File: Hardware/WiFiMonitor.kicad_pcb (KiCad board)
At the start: 2 copper layers, 47.2 x 47.1 mm, 41 parts, among them J1 ADAP_ESP, J2 FTDI, J3 BATT, U1 4N25, U2 4N25, U3 4N25, U4 4N25, U5 U5, U6 AP1117-33, U7 DS3231MZ+

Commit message: pads3
move
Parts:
- moved IN2 0.35 mm to (145.6, 97.8), turned to 136 degrees
- moved COM2 0.09 mm to (154.7, 84.7), turned to 134 degrees
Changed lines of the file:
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@@
     (area 125.549999 67.068854 174.355 116.145)
     (thickness 1.6)
-    (drawings 30)
-    (tracks 632)
+    (drawings 28)
+    (tracks 634)
     (zones 0)
     (modules 41)
@@
   )
   (module PADS:PAD_4X2mmTH (layer F.Cu)
-    (at 145.92 97.67 145)
-    (fp_text reference IN2 (at 0 2.5 145) (layer F.SilkS)
+    (at 145.59 97.8 136)
+    (fp_text reference IN2 (at 0 2.5 136) (layer F.SilkS)
       (effects (font (size 1 1) (thickness 0.15)))
     )
-    (fp_text value 1_IN (at 0 -2.5 145) (layer F.Fab)
+    (fp_text value 1_IN (at 0 -2.5 136) (layer F.Fab)
       (effects (font (size 1 1) (thickness 0.15)))
     )
-    (pad 1 thru_hole rect (at 0 0 145) (size 5 2) (drill oval 3.25 0.78) (layers *.Cu *.Mask)
+    (pad 1 thru_hole rect (at 0 0 136) (size 5 2) (drill oval 3.25 0.78) (layers *.Cu *.Mask)
       (net 11 "Net-(IN2-Pad1)"))
   )
@@
   )
   (module PADS:PAD_4X2mmTH (layer F.Cu)
-    (at 154.59 84.66 133)
-    (fp_text reference COM2 (at 0.082226 -2.078975 133) (layer F.SilkS)
+    (at 154.66 84.72 134)
+    (fp_text reference COM2 (at 0.082226 -2.078975 134) (layer F.SilkS)
       (effects (font (size 1 1) (thickness 0.15)))
     )
-    (fp_text value TORRETA (at 0 -2.5 133) (layer F.Fab)
+    (fp_text value TORRETA (at 0 -2.5 134) (layer F.Fab)
       (effects (font (size 1 1) (thickness 0.15)))
     )
-    (pad 1 thru_hole rect (at 0 0 133) (size 5 2) (drill oval 3.25 0.78) (layers *.Cu *.Mask)
+    (pad 1 thru_hole rect (at 0 0 134) (size 5 2) (drill oval 3.25 0.78) (layers *.Cu *.Mask)
       (net 6 GNDA))
   )
@@
     )
   )
-  (dimension 10.120835 (width 0.3) (layer Margin)
-    (gr_text "10.121 mm" (at 150.245462 94.674818 0.7359724973) (layer Margin)
-      (effects (font (size 1.5 1.5) (thickness 0.3)))
-    )
-    (feature1 (pts (xy 145.21 96.65) (xy 145.168122 93.38993)))
-    (feature2 (pts (xy 155.33 96.52) (xy 155.288122 93.25993)))
-    (crossbar (pts (xy 155.322803 95.959707) (xy 145.202803 96.089707)))
-    (arrow1a (pts (xy 145.202803 96.089707) (xy 146.321681 95.488865)))
-    (arrow1b (pts (xy 145.202803 96.089707) (xy 146.336746 96.66161)))
-    (arrow2a (pts (xy 155.322803 95.959707) (xy 154.18886 95.387804)))
-    (arrow2b (pts (xy 155.322803 95.959707) (xy 154.203925 96.560549)))
-  )
-  (dimension 5.11 (width 0.3) (layer Margin)
-    (gr_text "5 mm" (at 150.435 96.56) (layer Margin)
-      (effects (font (size 1.5 1.5) (thickness 0.3)))
-    )
-    (feature1 (pts (xy 147.88 98.58) (xy 147.88 95.21)))
-    (feature2 (pts (xy 152.99 98.58) (xy 152.99 95.21)))
-    (crossbar (pts (xy 152.99 97.91) (xy 147.88 97.91)))
-    (arrow1a (pts (xy 147.88 97.91) (xy 149.006504 97.323579)))
-    (arrow1b (pts (xy 147.88 97.91) (xy 149.006504 98.496421)))
-    (arrow2a (pts (xy 152.99 97.91) (xy 151.863496 97.323579)))
-    (arrow2b (pts (xy 152.99 97.91) (xy 151.863496 98.496421)))
-  )
   (gr_circle (center 149.85 91.06) (end 151.05 94.37) (layer Edge.Cuts) (width 0.2))
   (gr_circle (center 149.86 91.03) (end 153.19 93.27) (layer Margin) (width 0.2))
@@
   (segment (start 153.62 103.55) (end 155.175 103.55) (width 0.3) (layer B.Cu) (net 10))
   (segment (start 153.62 103.55) (end 154.95 103.55) (width 0.3) (layer B.Cu) (net 10))
+  (segment (start 144.44 99.15) (end 144.44 98.95) (width 0.3) (layer F.Cu) (net 11))
+  (segment (start 144.44 98.95) (end 145.59 97.8) (width 0.3) (layer F.Cu) (net 11))
   (segment (start 145.972894 101.89) (end 144.44 100.357106) (width 0.3) (layer F.Cu) (net 11))
   (segment (start 144.44 100.357106) (end 144.44 99.15) (width 0.3) (layer F.Cu) (net 11))
-  (segment (start 144.44 99.15) (end 145.92 97.67) (width 0.3) (layer F.Cu) (net 11))
   (segment (start 146.68 101.89) (end 145.972894 101.89) (width 0.3) (layer F.Cu) (net 11))
   (via (at 146.68 101.89) (size 1) (drill 0.4) (layers F.Cu B.Cu) (net 11))
@@
   (segment (start 135.53 103.045) (end 136.8206 103.045) (width 0.3) (layer F.Cu) (net 22))
   (segment (start 136.8206 103.045) (end 136.8356 103.06) (width 0.3) (layer F.Cu) (net 22))
-  (segment (start 160.23 93.59) (end 160.23 84.56) (width 0.3) (layer F.Cu) (net 23))
-  (segment (start 160.23 84.56) (end 159.86 84.19) (width 0.3) (layer F.Cu) (net 23))
-  (segment (start 159.86 84.19) (end 159.86 75.9) (width 0.3) (layer F.Cu) (net 23))
-  (segment (start 163.69 98.88) (end 160.23 95.42) (width 0.3) (layer B.Cu) (net 23))
-  (segment (start 160.23 95.42) (end 160.23 93.59) (width 0.3) (layer B.Cu) (net 23))
-  (via (at 160.23 93.59) (size 1) (drill 0.4) (layers F.Cu B.Cu) (net 23))
-  (segment (start 163.69 98.98) (end 163.69 98.88) (width 0.3) (layer B.Cu) (net 23))
   (segment (start 143.51 106.21) (end 144.61 106.21) (width 0.3) (layer B.Cu) (net 23))
-  (segment (start 144.61 106.21) (end 145.11 105.71) (width 0.3) (layer B.Cu) (net 23))
   (segment (start 145.11 105.71) (end 145.11 101.765) (width 0.3) (layer B.Cu) (net 23))
-  (segment (start 163.25 100.58) (end 163.69 100.14) (width 0.3) (layer B.Cu) (net 23))
-  (segment (start 145.11 101.765) (end 146.16 100.715) (width 0.3) (layer B.Cu) (net 23))
-  (segment (start 146.16 100.715) (end 153.885 100.715) (width 0.3) (layer B.Cu) (net 23))
-  (segment (start 154.86 99.74) (end 158 99.74) (width 0.3) (layer B.Cu) (net 23))
-  (segment (start 153.885 100.715) (end 154.86 99.74) (width 0.3) (layer B.Cu) (net 23))
+  (segment (start 144.61 106.21) (end 145.11 105.71) (width 0.3) (layer B.Cu) (net 23))
+  (segment (start 150.52789 100.86499) (end 153.73501 100.86499) (width 0.3) (layer B.Cu) (net 23))
+  (segment (start 160.23 95.42) (end 160.23 93.59) (width 0.3) (layer B.Cu) (net 23))
+  (segment (start 145.11 101.765) (end 145.945 100.93) (width 0.3) (layer B.Cu) (net 23))
+  (segment (start 145.945 100.93) (end 150.46288 100.93) (width 0.3) (layer B.Cu) (net 23))
+  (segment (start 150.46288 100.93) (end 150.52789 100.86499) (width 0.3) (layer B.Cu) (net 23))
+  (segment (start 153.73501 100.86499) (end 154.86 99.74) (width 0.3) (layer B.Cu) (net 23))
   (segment (start 158 99.74) (end 158.84 100.58) (width 0.3) (layer B.Cu) (net 23))
+  (segment (start 154.86 99.74) (end 158 99.74) (width 0.3) (layer B.Cu) (net 23))
   (segment (start 158.84 100.58) (end 163.25 100.58) (width 0.3) (layer B.Cu) (net 23))
-  (segment (start 163.69 100.14) (end 163.69 98.98) (width 0.3) (layer B.Cu) (net 23))
+  (segment (start 163.69 100.14) (end 163.69 98.88) (width 0.3) (layer B.Cu) (net 23))
+  (segment (start 163.25 100.58) (end 163.69 100.14) (width 0.3) (layer B.Cu) (net 23))
+  (segment (start 163.69 98.88) (end 160.23 95.42) (width 0.3) (layer B.Cu) (net 23))
+  (segment (start 160.23 93.59) (end 160.23 84.56) (width 0.3) (layer F.Cu) (net 23))
+  (segment (start 160.23 84.56) (end 159.86 84.19) (width 0.3) (layer F.Cu) (net 23))
+  (segment (start 159.86 84.19) (end 159.86 75.9) (width 0.3) (layer F.Cu) (net 23))
+  (via (at 160.23 93.59) (size 1) (drill 0.4) (layers F.Cu B.Cu) (net 23))
   (segment (start 148.749999 106.749999) (end 149.185 106.749999) (width 0.3) (layer F.Cu) (net 24))
   (segment (start 149.185 106.749999) (end 157.475001 106.749999) (width 0.3) (layer F.Cu) (net 24))

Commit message: pads4
move
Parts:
- moved COM2 0.54 mm to (154.2, 84.4), turned to 140 degrees
- moved IN2 0.34 mm to (145.7, 98.1), turned to 145 degrees
- moved COM1 0.26 mm to (145.6, 84.5)
- moved IN1 0.21 mm to (154.4, 97.6)
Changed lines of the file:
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@@
     (links 70)
     (no_connects 0)
-    (area 125.549999 67.068854 174.355 116.145)
+    (area 126.056132 67.439999 173.398541 114.790001)
     (thickness 1.6)
     (drawings 28)
@@
   )
   (module PADS:PAD_4X2mmTH (layer F.Cu)
-    (at 145.59 97.8 136)
-    (fp_text reference IN2 (at 0 2.5 136) (layer F.SilkS)
+    (at 145.69 98.12 145)
+    (fp_text reference IN2 (at 0 2.5 145) (layer F.SilkS)
       (effects (font (size 1 1) (thickness 0.15)))
     )
-    (fp_text value 1_IN (at 0 -2.5 136) (layer F.Fab)
+    (fp_text value 1_IN (at 0 -2.5 145) (layer F.Fab)
       (effects (font (size 1 1) (thickness 0.15)))
     )
-    (pad 1 thru_hole rect (at 0 0 136) (size 5 2) (drill oval 3.25 0.78) (layers *.Cu *.Mask)
+    (pad 1 thru_hole rect (at 0 0 145) (size 5 2) (drill oval 3.25 0.78) (layers *.Cu *.Mask)
       (net 11 "Net-(IN2-Pad1)"))
   )
@@
   )
   (module PADS:PAD_4X2mmTH (layer F.Cu)
-    (at 154.19 97.57 41)
+    (at 154.39 97.62 41)
     (fp_text reference IN1 (at -0.119133 -2.4083 41) (layer F.SilkS)
       (effects (font (size 1 1) (thickness 0.15)))
@@
   )
   (module PADS:PAD_4X2mmTH (layer F.Cu)
-    (at 145.29 84.49 40)
+    (at 145.55 84.5 40)
     (fp_text reference COM1 (at 0 2.5 40) (layer F.SilkS)
       (effects (font (size 1 1) (thickness 0.15)))
@@
   )
   (module PADS:PAD_4X2mmTH (layer F.Cu)
-    (at 154.66 84.72 134)
-    (fp_text reference COM2 (at 0.082226 -2.078975 134) (layer F.SilkS)
+    (at 154.22 84.41 140)
+    (fp_text reference COM2 (at 0.082226 -2.078975 140) (layer F.SilkS)
       (effects (font (size 1 1) (thickness 0.15)))
     )
-    (fp_text value TORRETA (at 0 -2.5 134) (layer F.Fab)
+    (fp_text value TORRETA (at 0 -2.5 140) (layer F.Fab)
       (effects (font (size 1 1) (thickness 0.15)))
     )
-    (pad 1 thru_hole rect (at 0 0 134) (size 5 2) (drill oval 3.25 0.78) (layers *.Cu *.Mask)
+    (pad 1 thru_hole rect (at 0 0 140) (size 5 2) (drill oval 3.25 0.78) (layers *.Cu *.Mask)
       (net 6 GNDA))
   )
@@
   (segment (start 153.62 103.55) (end 155.175 103.55) (width 0.3) (layer B.Cu) (net 10))
   (segment (start 153.62 103.55) (end 154.95 103.55) (width 0.3) (layer B.Cu) (net 10))
-  (segment (start 144.44 99.15) (end 144.44 98.95) (width 0.3) (layer F.Cu) (net 11))
-  (segment (start 144.44 98.95) (end 145.59 97.8) (width 0.3) (layer F.Cu) (net 11))
+  (segment (start 144.44 100.357106) (end 144.44 99.7) (width 0.3) (layer F.Cu) (net 11))
+  (segment (start 144.44 99.7) (end 144.44 99.2) (width 0.3) (layer F.Cu) (net 11))
+  (segment (start 144.44 99.2) (end 145.47 98.17) (width 0.3) (layer F.Cu) (net 11))
   (segment (start 145.972894 101.89) (end 144.44 100.357106) (width 0.3) (layer F.Cu) (net 11))
-  (segment (start 144.44 100.357106) (end 144.44 99.15) (width 0.3) (layer F.Cu) (net 11))
   (segment (start 146.68 101.89) (end 145.972894 101.89) (width 0.3) (layer F.Cu) (net 11))
   (via (at 146.68 101.89) (size 1) (drill 0.4) (layers F.Cu B.Cu) (net 11))

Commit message: pads4_1
edge board
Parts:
- moved J1 1.00 mm to (132.9, 87.3)
- moved D1 0.91 mm to (135.3, 81.8)
- moved S2 0.71 mm to (129.1, 88.8)
- moved U7 0.32 mm to (132.9, 104.0)
- moved C3 0.29 mm to (140.3, 78.1)
- moved R17 0.17 mm to (137.9, 78.2)
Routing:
- net /D2: track 78.3 -> 73.0 mm
- net +3V3: track 157.5 -> 159.8 mm
- net /D0: track 87.4 -> 86.1 mm
- net /RX: track 24.2 -> 25.3 mm
- net /D1: track 66.1 -> 65.2 mm
- net /D3: track 75.4 -> 74.6 mm
- net /TX: track 25.0 -> 25.9 mm
- net /GPIO0: track 5.63 -> 6.42 mm
- net /SCL: track 2.83 -> 2.14 mm
- net /SDA: track 10.0 -> 9.49 mm
- net GND: track 160.9 -> 161.2 mm, vias 6 -> 7
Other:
- outline, holes or cut-outs redrawn

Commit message: pads4_2
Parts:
- moved U3 0.50 mm to (164.8, 104.0)
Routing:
- net /D2: track 73.0 -> 79.4 mm
- net /D3: track 74.6 -> 75.6 mm
- net GNDA: track 83.9 -> 82.9 mm
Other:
- outline, holes or cut-outs redrawn

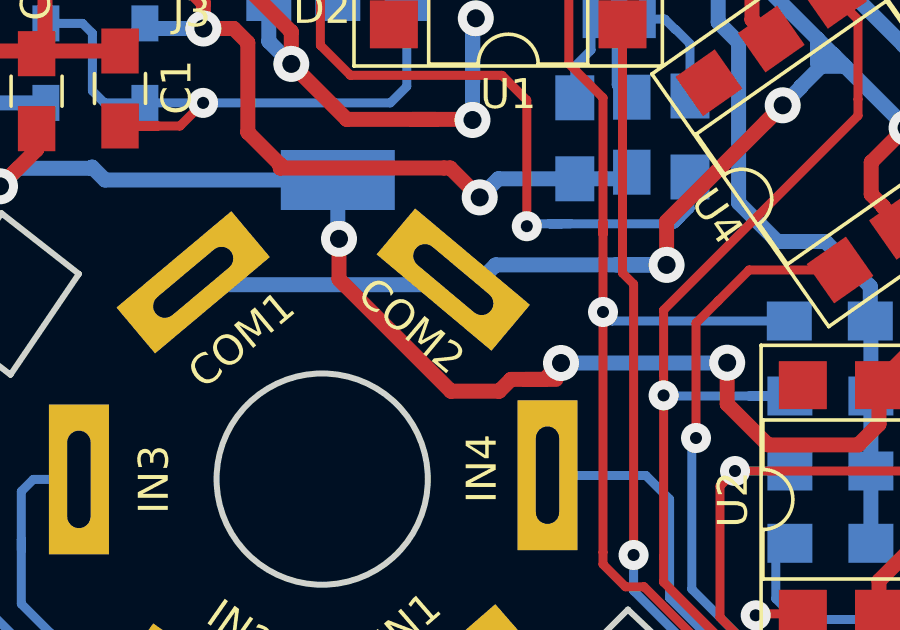
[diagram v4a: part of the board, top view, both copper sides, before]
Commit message: pads4_21
move
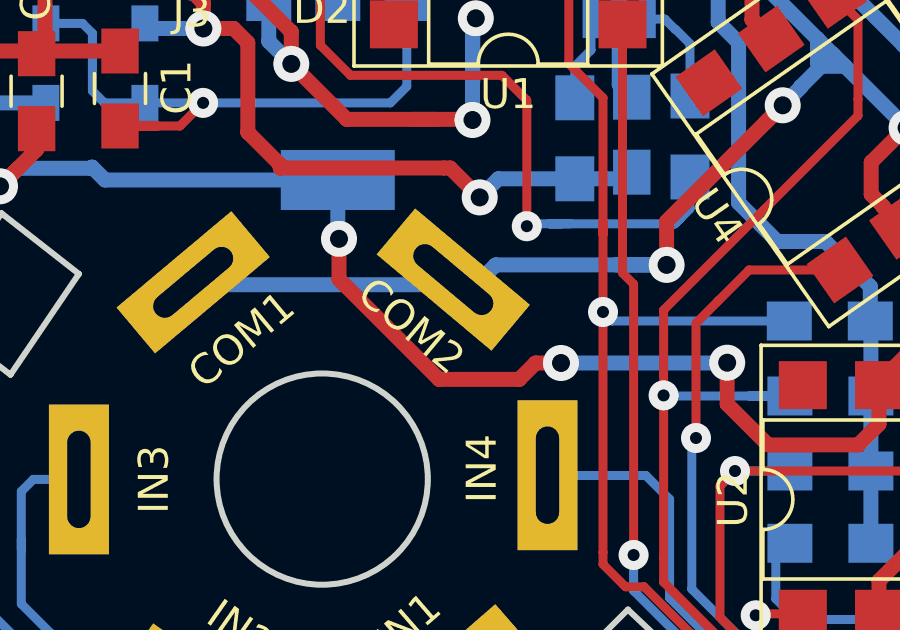
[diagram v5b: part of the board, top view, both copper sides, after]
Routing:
- net +3V3: track 159.8 -> 158.4 mm
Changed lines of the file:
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@@
     (links 70)
     (no_connects 2)
-    (area 126.056132 67.439999 173.398541 114.790001)
+    (area 125.549999 67.068854 174.355 116.145)
     (thickness 1.6)
     (drawings 29)
-    (tracks 650)
+    (tracks 647)
     (zones 0)
     (modules 41)
@@
   (segment (start 144.11 76.04) (end 143.94 75.87) (width 0.5) (layer B.Cu) (net 4))
   (via (at 145.89 76.04) (size 1.2) (drill 0.6) (layers F.Cu B.Cu) (net 4))
+  (segment (start 157.81 87.19) (end 156.961472 87.19) (width 0.5) (layer F.Cu) (net 5))
+  (segment (start 156.961472 87.19) (end 156.414469 87.737003) (width 0.5) (layer F.Cu) (net 5))
+  (segment (start 156.414469 87.737003) (end 153.747003 87.737003) (width 0.5) (layer F.Cu) (net 5))
+  (segment (start 153.747003 87.737003) (end 150.41 84.4) (width 0.5) (layer F.Cu) (net 5))
+  (segment (start 150.41 84.4) (end 150.41 83.05) (width 0.5) (layer F.Cu) (net 5))
   (segment (start 134.95 84.63) (end 134.73 84.63) (width 0.5) (layer F.Cu) (net 5))
   (segment (start 135.44 85.13) (end 135.44 85.12) (width 0.5) (layer F.Cu) (net 5))
@@
   (segment (start 157.81 87.19) (end 163.34 87.19) (width 0.5) (layer B.Cu) (net 5))
   (segment (start 163.34 87.19) (end 163.35 87.18) (width 0.5) (layer B.Cu) (net 5))
-  (segment (start 156.63 87.737003) (end 157.642997 87.737003) (width 0.5) (layer F.Cu) (net 5))
-  (segment (start 156.142997 87.737003) (end 156.63 87.737003) (width 0.5) (layer F.Cu) (net 5))
-  (segment (start 156.63 87.737003) (end 157.262997 87.737003) (width 0.5) (layer F.Cu) (net 5))
-  (segment (start 157.262997 87.737003) (end 157.81 87.19) (width 0.5) (layer F.Cu) (net 5))
   (via (at 157.81 87.19) (size 1.2) (drill 0.6) (layers F.Cu B.Cu) (net 5))
-  (segment (start 150.41 83.05) (end 150.41 84.4) (width 0.5) (layer F.Cu) (net 5))
-  (segment (start 150.41 84.4) (end 154.14 88.13) (width 0.5) (layer F.Cu) (net 5))
-  (segment (start 154.14 88.13) (end 155.75 88.13) (width 0.5) (layer F.Cu) (net 5))
-  (segment (start 155.75 88.13) (end 156.142997 87.737003) (width 0.5) (layer F.Cu) (net 5))
   (segment (start 164.71 89.92) (end 163.35 88.56) (width 0.5) (layer F.Cu) (net 5))
   (segment (start 163.35 88.56) (end 163.35 87.18) (width 0.5) (layer F.Cu) (net 5))
